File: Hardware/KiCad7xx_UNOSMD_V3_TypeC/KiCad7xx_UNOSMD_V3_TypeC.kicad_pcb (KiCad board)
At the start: 2 copper layers, 68.6 x 53.3 mm, 76 parts, among them J1 -, J2 -, T1 FDN340P, U1 NCP1117ST50T3G, U2 LP2985-33DBVR, U3 16U2, U4 ATMEGA328P-MU, U5 LMV358IDGKR, X1 POWERSUPPLY_DC21MMX, X2 USB-B_TH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

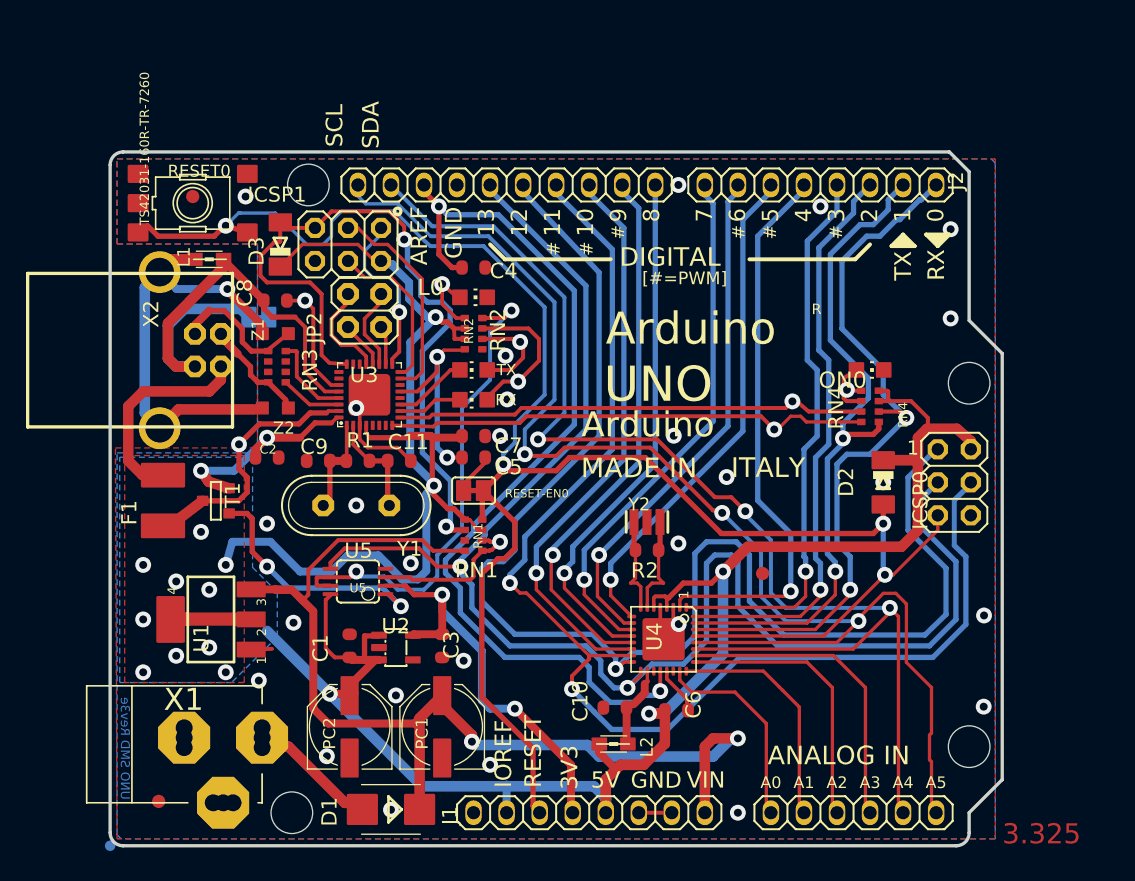
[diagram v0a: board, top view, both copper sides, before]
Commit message: Add:TypeC connector was added to the board data.
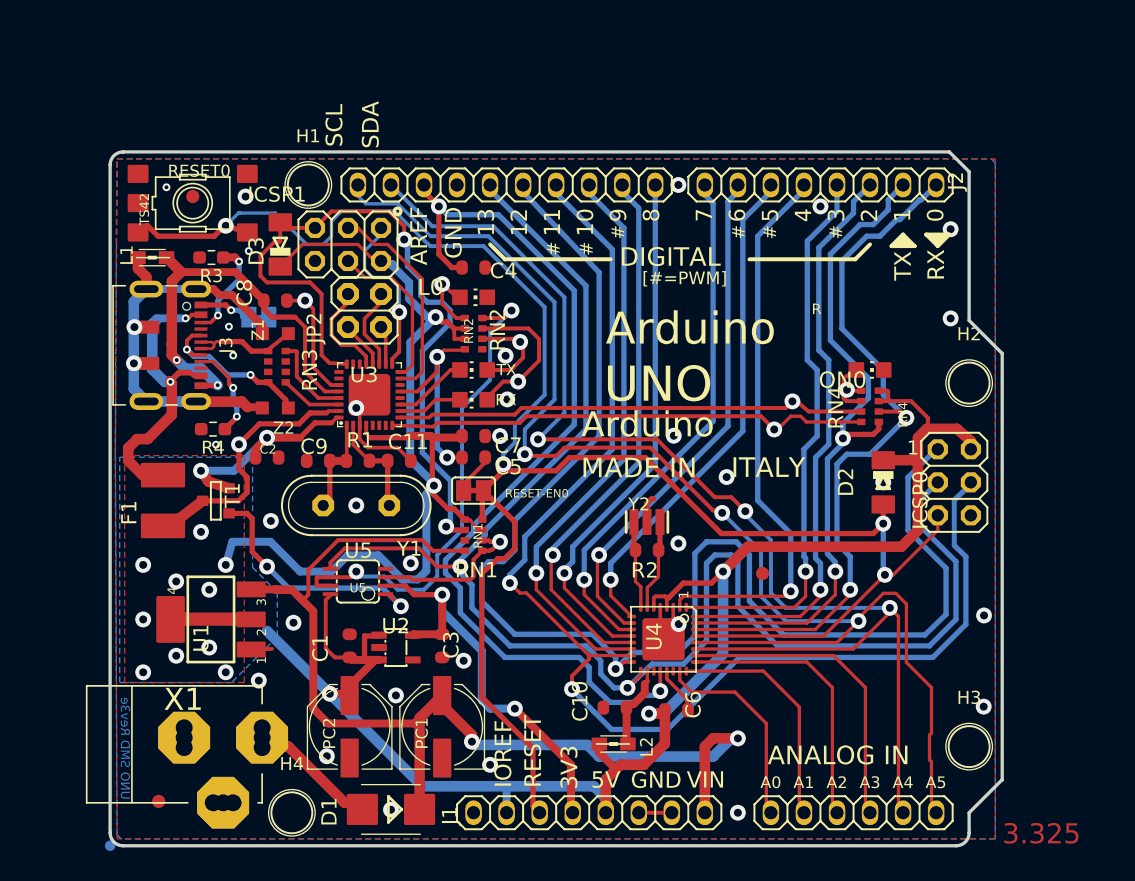
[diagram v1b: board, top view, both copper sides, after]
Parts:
- removed @HOLE0, @HOLE1, @HOLE2, @HOLE3: , 
- removed FRAME1: DNP, UNOSMD_V3:FRAME
- removed TP_USH0: TP_SP, UNOSMD_V3:TP-SP
- removed X2: USB-B_TH, UNOSMD_V3:PN61729
- added H1: MountingHole, MountingHole:MountingHole_3.2mm_M3_ISO14580, F.Cu at (129.4, 80.9)
- added H2: MountingHole, MountingHole:MountingHole_3.2mm_M3_ISO14580, F.Cu at (180.2, 96.1)
- added H3: MountingHole, MountingHole:MountingHole_3.2mm_M3_ISO14580, F.Cu at (180.2, 124.0)
- added H4: MountingHole, MountingHole:MountingHole_3.2mm_M3_ISO14580, F.Cu at (128.2, 129.1)
- added J3: USB_C_Receptacle_USB2.0, Connector_USB:USB_C_Receptacle_JAE_DX07S016JA1R1500, F.Cu at (118.1, 93.2)
- added R3: 5.1k, Resistor_SMD:R_0603_1608Metric_Pad0.98x0.95mm_HandSolder, F.Cu at (122.0, 86.5)
- added R4: 5.1k, Resistor_SMD:R_0603_1608Metric_Pad0.98x0.95mm_HandSolder, F.Cu at (122.1, 99.6)
- FD1, FD2, FD3: value DNP -> FIDUCIAL-1.5MM
- GROUND0, RESET-EN0: value (none) -> SJ
- J2: value - -> PINHD-1X18
- RESET0: value TS42031-160R-TR-7260 -> TS42
- U1: value NCP1117ST50T3G -> MC33269ST
- U2: value LP2985-33DBVR -> LP2985-XXDBVR
- U3: value 16U2 -> ATMEGA16U2
- U4: value ATMEGA328P-MU -> ATMEGAXX8-MUR
- U5: value LMV358IDGKR -> LMV358?MM
- Y2: value CSTCE16M0V53-R0 16MHZ -> RESONATORMU
- Z1, Z2: value CG0603MLC-05E -> VARISTORCN0603
- moved L1 4.38 mm to (117.5, 86.5)
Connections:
- net A0 renamed /A0
- net A1 renamed /A1
- net A2 renamed /A2
- net A3 renamed /A3
- net A4/SDA renamed /A4/SDA
- net A5/SCL renamed /A5/SCL
- net AREF renamed /AREF
- net CMP renamed /CMP
- net D+ renamed /D+
- net D- renamed /D-
- net DTR renamed /DTR
- net GATE_CMD renamed /GATE_CMD
- net IO0 renamed /IO0
- net IO1 renamed /IO1
- net IO2 renamed /IO2
- net IO3 renamed /IO3
- net IO4 renamed /IO4
- net IO5 renamed /IO5
- net IO6 renamed /IO6
- net IO7 renamed /IO7
- net IO8 renamed /IO8
- net IO9 renamed /IO9
- net L13 renamed /L13
- net M8RXD renamed /M8RXD
- net M8TXD renamed /M8TXD
- net MISO renamed /MISO
- net MISO2 renamed /MISO2
- net MOSI renamed /MOSI
- net MOSI2 renamed /MOSI2
- net PB4 renamed /PB4
- net PB5 renamed /PB5
- net PB6 renamed /PB6
- net PB7 renamed /PB7
- net PWRIN renamed /PWRIN
- net RD+ renamed /RD+
- net RD- renamed /RD-
- net RESET renamed /RESET
- net RESET2 renamed /RESET2
- net RXLED renamed /RXLED
- net SCK renamed /SCK
- net SCK2 renamed /SCK2
- net SS renamed /SS
- net TP_VUCAP renamed /TP_VUCAP
- net TXLED renamed /TXLED
- net UGND renamed /UGND
- net USBVCC renamed /USBVCC
- net USHIELD renamed /USHIELD
- net XT1 renamed /XT1
- net XT2 renamed /XT2
- net XTAL1 renamed /XTAL1
- net XTAL2 renamed /XTAL2
- F1 pad 2: XUSB -> /XUSB
- J1 pad 1: (no net) -> unconnected-(J1-Pad1)
- ORIGIN0 pad X: (no net) -> unconnected-(ORIGIN0-TESTP-PadX)
- RN3 pad 2: (no net) -> unconnected-(RN3B-1-Pad2)
- RN3 pad 3: (no net) -> unconnected-(RN3C-1-Pad3)
- RN3 pad 6: (no net) -> unconnected-(RN3C-2-Pad6)
- RN3 pad 7: (no net) -> unconnected-(RN3B-2-Pad7)
- U2 pad 4: (no net) -> unconnected-(U2-NC/FB-Pad4)
- U3 pad 12: (no net) -> unconnected-(U3-(RTS/AIN5/INT6)PD6-Pad12)
- U3 pad 14: (no net) -> unconnected-(U3-(SS/PCINT0)PB0-Pad14)
- U3 pad 22: (no net) -> unconnected-(U3-(INT4/ICP1/CLK0)PC7-Pad22)
- U3 pad 23: (no net) -> unconnected-(U3-(OC1A/PCINT8)PC6-Pad23)
- U3 pad 25: (no net) -> unconnected-(U3-(PCINT9/OC1B)PC5-Pad25)
- U3 pad 26: (no net) -> unconnected-(U3-(PCINT10)PC4-Pad26)
- U3 pad 5: (no net) -> unconnected-(U3-(AIN2/PCINT11)PC2-Pad5)
- U3 pad 6: (no net) -> unconnected-(U3-(OC0B/INT0)PD0-Pad6)
- U3 pad 7: (no net) -> unconnected-(U3-(AIN0/INT1)PD1-Pad7)
- U4 pad 19: (no net) -> unconnected-(U4-ADC6-Pad19)
- U4 pad 22: (no net) -> unconnected-(U4-ADC7-Pad22)
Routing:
- net /XUSB: track 0.00 -> 23.4 mm, vias 0 -> 2
- net XUSB: track 16.3 -> 0.00 mm
- net Net-(J3-CC1): track 0.00 -> 7.70 mm, vias 0 -> 2
- net Net-(J3-CC2): track 0.00 -> 7.27 mm, vias 0 -> 2
- net /D-: track 8.26 -> 13.2 mm, vias 0 -> 2
- net /UGND: track 39.2 -> 36.1 mm, vias 0 -> 3
- net /USHIELD: track 34.9 -> 32.0 mm, vias 1 -> 2
- net GND: track 22.1 -> 24.2 mm, vias 27 -> 32
- net /D+: track 10.8 -> 9.01 mm
- net /XTAL1: track 7.81 -> 6.98 mm
- net /XTAL2: track 7.40 -> 6.78 mm
